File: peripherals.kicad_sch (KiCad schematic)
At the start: 93 parts, among them J10 Molex_PicoBlade_1x4_0533980471, J11 ERF8-040-05.0-L-DV-K-TR, J14 JST_SH_1x4_SM04B-SRSS-TB-LF-SN, J9 TagConnect_2x5_P1.27mm_TC2050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, Q10 PJE138K, Q9 PJE138K, U30 TPD4E05U06QDQARQ1, U33 NTS0102_XSON, U34 PCAL6408A_VQFN, U35 AP22653_DFN

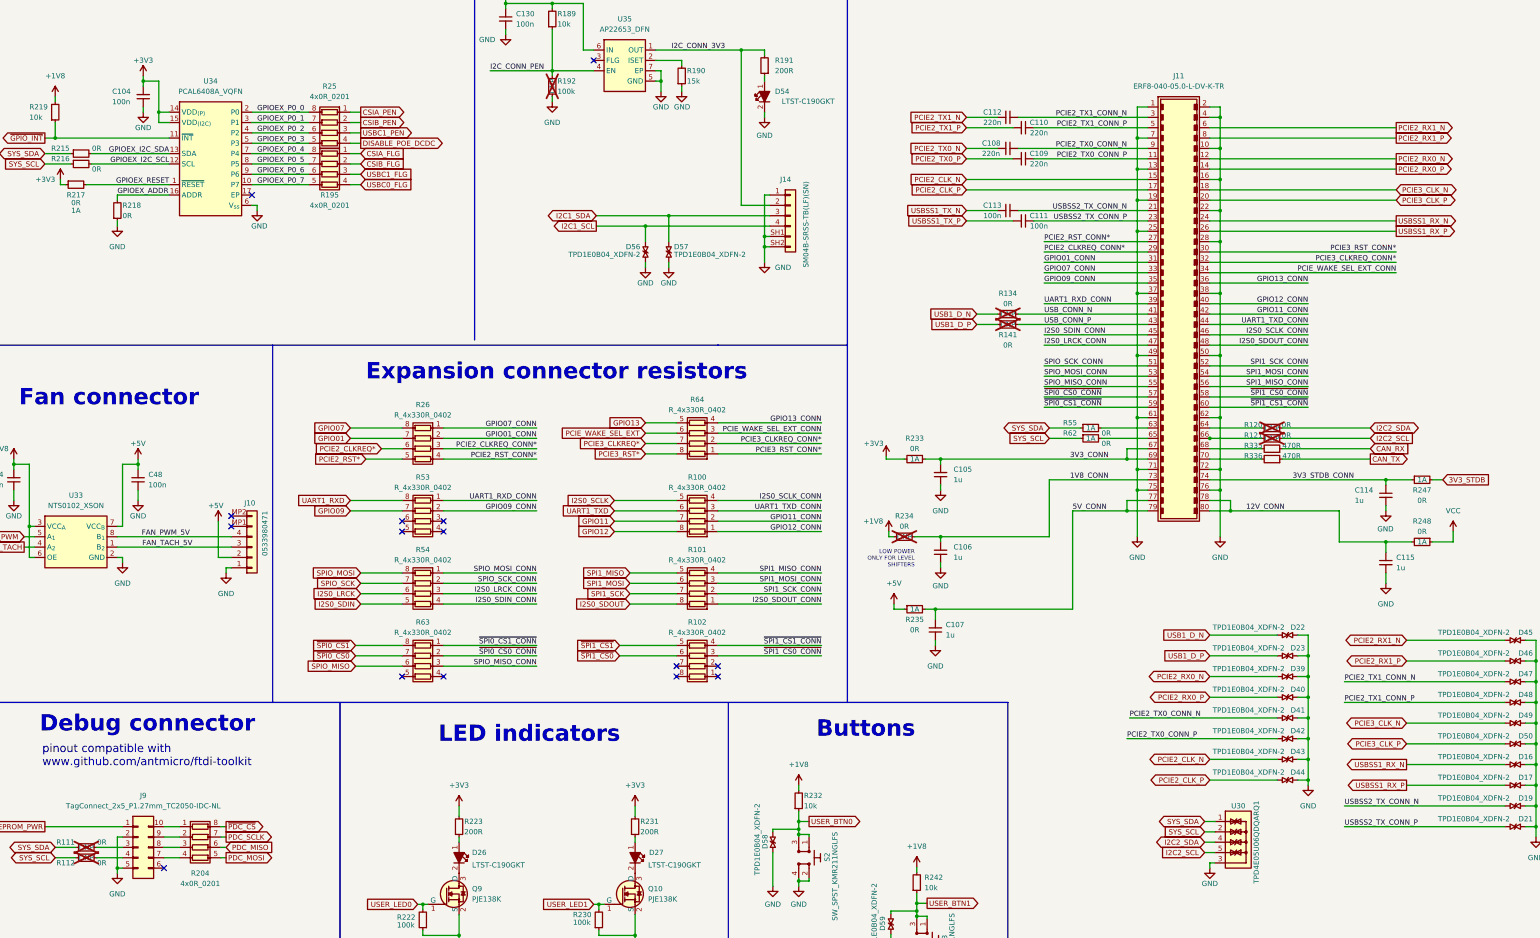
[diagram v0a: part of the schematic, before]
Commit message: 5/16 Commit: Sch Mods added and beginning Development on PCB layout
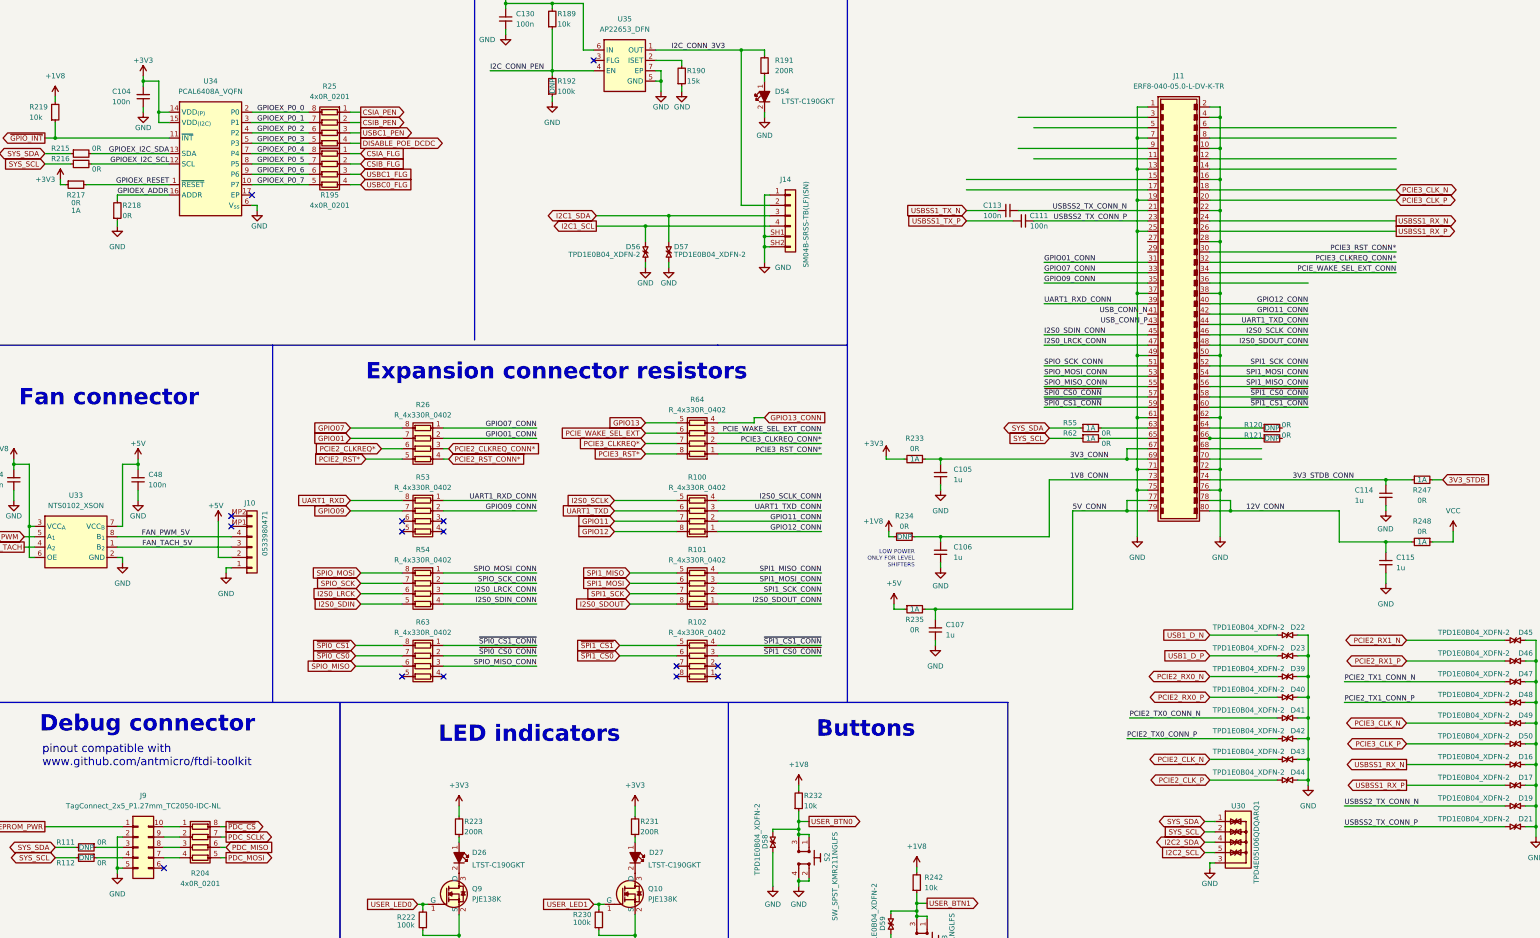
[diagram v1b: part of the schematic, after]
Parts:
- removed C108, C109, C110, C112: C_220n_0402, jetson-orin-baseboard-footprints:C_0402_1005Metric, symbol jetson-orin-baseboard:C_220n_0402
- removed R134, R141: R_0R_0402, jetson-orin-baseboard-footprints:R_0402_1005Metric, symbol jetson-orin-baseboard:R_0R_0402
- removed R335, R336: R_470R_0402, jetson-orin-baseboard-footprints:R_0402_1005Metric, symbol jetson-orin-baseboard:R_470R_0402
- R111, R112, R120, R121, R192, R234: now fitted
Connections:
- net GPIO13_CONN: no longer J11.36
- net I2C2_SCL: no longer R121.2
- net I2C2_SDA: no longer R120.2
- net PCIE2_CLKREQ_CONN*: no longer J11.29
- net PCIE2_CLK_N: no longer J11.15
- net PCIE2_CLK_P: no longer J11.17
- net PCIE2_RST_CONN*: no longer J11.27
- net PCIE2_RX0_N: no longer J11.12
- net PCIE2_RX0_P: no longer J11.14
- net PCIE2_RX1_N: no longer J11.6
- net PCIE2_RX1_P: no longer J11.8
- net PCIE2_TX0_CONN_N: no longer J11.9
- net PCIE2_TX0_CONN_P: no longer J11.11
- net PCIE2_TX1_CONN_N: no longer J11.3
- net PCIE2_TX1_CONN_P: no longer J11.5
